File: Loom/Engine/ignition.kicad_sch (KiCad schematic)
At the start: 0 parts

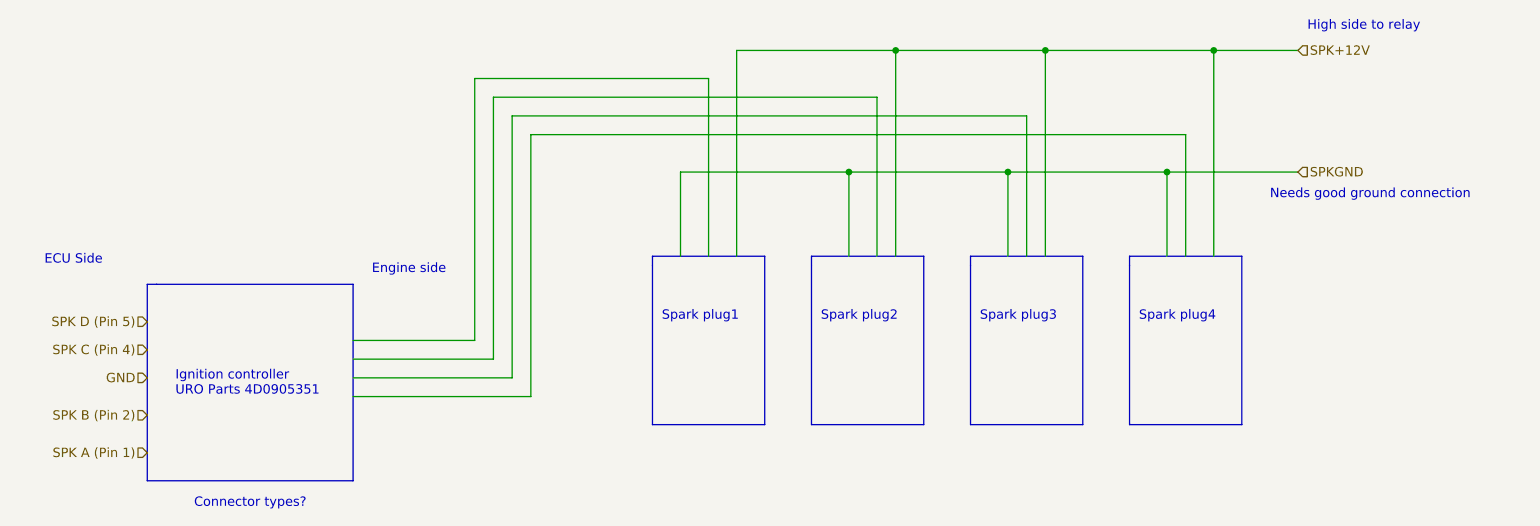
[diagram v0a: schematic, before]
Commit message: Changes to the injector numbering
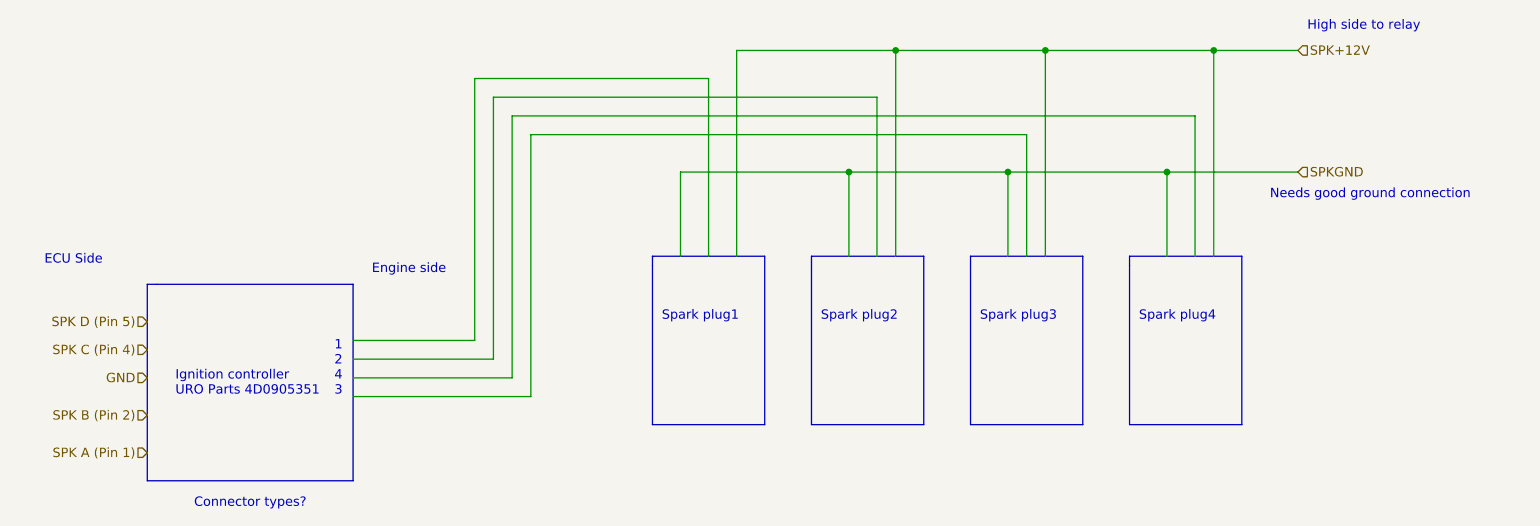
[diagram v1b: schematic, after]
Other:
- note added: "1 2 4 3"
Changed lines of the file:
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@@
     (stroke (width 0) (type default))
   )
-  (wire (pts (xy 214.63 66.04) (xy 144.78 66.04))
+  (wire (pts (xy 144.78 66.04) (xy 237.49 66.04))
     (stroke (width 0) (type default))
   )
@@
     (stroke (width 0) (type default))
   )
-  (wire (pts (xy 236.22 68.58) (xy 147.32 68.58))
-    (stroke (width 0) (type default))
-  )
   (wire (pts (xy 217.17 57.15) (xy 240.03 57.15))
     (stroke (width 0) (type default))
@@
     (stroke (width 0) (type default))
   )
-  (wire (pts (xy 236.22 85.09) (xy 236.22 68.58))
-    (stroke (width 0) (type default))
-  )
   (wire (pts (xy 194.31 85.09) (xy 194.31 63.5))
     (stroke (width 0) (type default))
@@
     (stroke (width 0) (type default))
   )
-  (wire (pts (xy 214.63 85.09) (xy 214.63 66.04))
+  (wire (pts (xy 214.63 68.58) (xy 147.32 68.58))
+    (stroke (width 0) (type default))
+  )
+  (wire (pts (xy 214.63 85.09) (xy 214.63 68.58))
     (stroke (width 0) (type default))
   )
@@
   )
   (polyline (pts (xy 228.6 107.95) (xy 243.84 107.95))
+    (stroke (width 0) (type default))
+  )
+  (wire (pts (xy 237.49 66.04) (xy 237.49 85.09))
     (stroke (width 0) (type default))
   )
@@
     (effects (font (size 1.27 1.27)) (justify left bottom))
   )
+  (text "1\n2\n4\n3" (at 120.65 104.14 0)
+    (effects (font (size 1.27 1.27)) (justify left bottom))
+  )
